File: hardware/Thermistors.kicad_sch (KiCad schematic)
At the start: 10 parts, among them J1 Conn_01x08

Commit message: updated sheets and 1st review changes
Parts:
- removed J1: Conn_01x08, symbol Connector_Generic:Conn_01x08
- removed R93, R94, R95, R96: 10k, symbol Device:R_Small
- added C1, C10, C11, C12, C2, C7, C8, C9: 1uF, symbol Device:C_Small
- added R33, R37, R38, R43, R44, R49, R50: 15k, symbol Device:R_Small
- added R34, R39, R40, R45, R46, R51, R52: 3.6k, symbol Device:R_Small
- added R35, R36, R41, R42, R47, R48: 1k, symbol Device:R_Small
- R29: value 10k -> 3.6k
- R30: value 10k -> 15k
- R31, R32: value 10k -> 1k
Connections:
- net NTC0: now also R48.1, R50.2, R52.1
- net NTC1: now also R47.1, R49.2, R51.1
- net NTC2: now also R42.1, R44.2, R46.1
- net NTC3: now also R41.1, R43.2, R45.1
- net NTC4: now also R36.1, R38.2, R40.1; no longer R32.1
- net NTC5: now also R35.1, R37.2, R39.1; no longer R31.1
- net NTC6: now also R32.1, R33.2, R34.1; no longer R30.1
- net NTC7: now also R30.2, R31.1
- net TSREF: now also R34.2, R39.2, R40.2, R45.2, R46.2, R51.2, R52.2; no longer R30.2, R31.2, R32.2
- net GNDA renamed AVSS
- net AVSS: now also R30.1, C1.2, C10.2, C11.2, C12.2, C2.2, C7.2, C8.2, C9.2, R33.1, R37.1, R38.1, R43.1, R44.1, R49.1, R50.1
- new net TEMP_0: C12.1, R48.2
- new net TEMP_1: C11.1, R47.2
- new net TEMP_2: C10.1, R42.2
- new net TEMP_3: C9.1, R41.2
- new net TEMP_4: C8.1, R36.2
- new net TEMP_5: C7.1, R35.2
- new net TEMP_6: C2.1, R32.2
- new net TEMP_7: C1.1, R31.2
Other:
- removed sheet 3V3_LDO
- removed sheet Temp Filters1
- moved on the sheet: C127

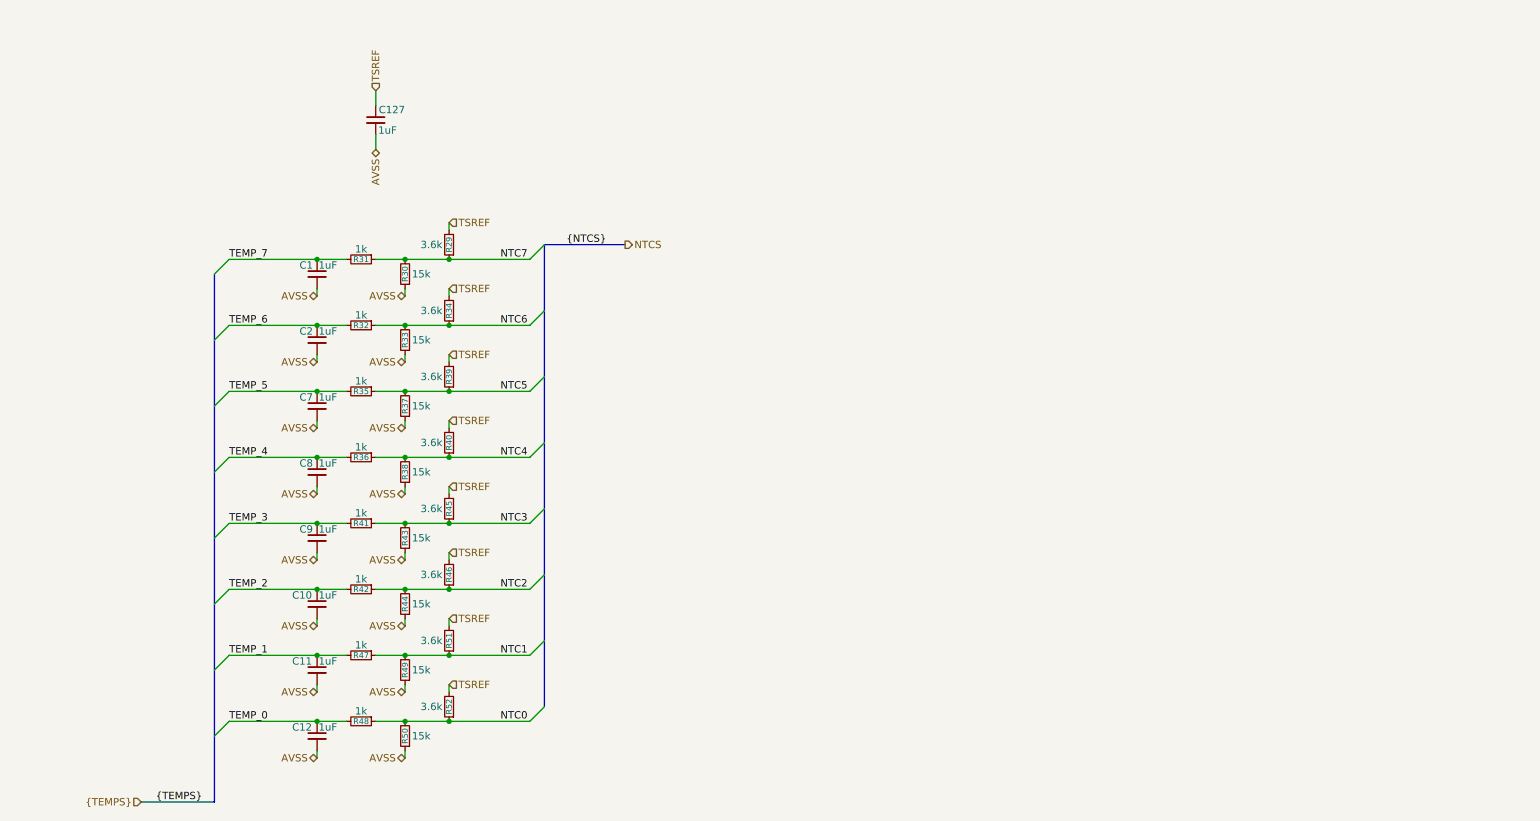
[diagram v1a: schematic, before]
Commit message: updated sheets, footprint, and calcs; 2nd review changes
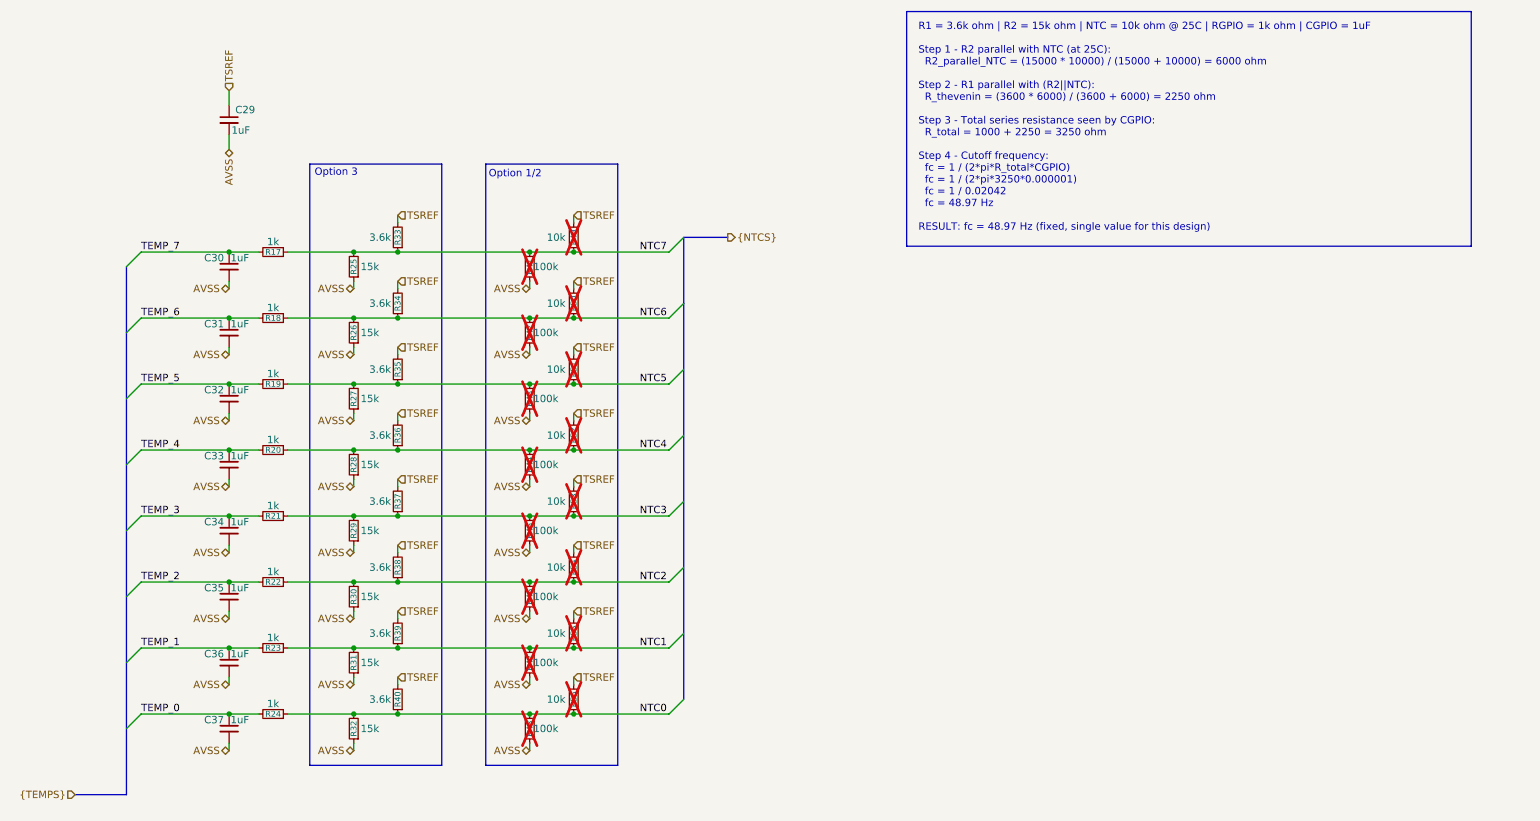
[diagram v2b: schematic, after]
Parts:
- added R41, R42, R43, R44, R45, R46, R47, R48: 100k, Resistor_SMD:R_0603_1608Metric_Pad0.98x0.95mm_HandSolder, symbol Device:R_Small
- added R49, R50, R51, R52, R53, R54, R55, R56: 10k, Resistor_SMD:R_0603_1608Metric_Pad0.98x0.95mm_HandSolder, symbol Device:R_Small
- C29: renamed from C127; footprint (none) -> Capacitor_SMD:C_0603_1608Metric_Pad1.08x0.95mm_HandSolder
- C30: renamed from C1; footprint (none) -> Capacitor_SMD:C_0603_1608Metric_Pad1.08x0.95mm_HandSolder
- C31: renamed from C2; footprint (none) -> Capacitor_SMD:C_0603_1608Metric_Pad1.08x0.95mm_HandSolder
- C32: renamed from C7; footprint (none) -> Capacitor_SMD:C_0603_1608Metric_Pad1.08x0.95mm_HandSolder
- C33: renamed from C8; footprint (none) -> Capacitor_SMD:C_0603_1608Metric_Pad1.08x0.95mm_HandSolder
- C34: renamed from C9; footprint (none) -> Capacitor_SMD:C_0603_1608Metric_Pad1.08x0.95mm_HandSolder
- C35: renamed from C10; footprint (none) -> Capacitor_SMD:C_0603_1608Metric_Pad1.08x0.95mm_HandSolder
- C36: renamed from C11; footprint (none) -> Capacitor_SMD:C_0603_1608Metric_Pad1.08x0.95mm_HandSolder
- C37: renamed from C12; footprint (none) -> Capacitor_SMD:C_0603_1608Metric_Pad1.08x0.95mm_HandSolder
- R17: renamed from R31; footprint (none) -> Resistor_SMD:R_0603_1608Metric_Pad0.98x0.95mm_HandSolder
- R18: renamed from R32; footprint (none) -> Resistor_SMD:R_0603_1608Metric_Pad0.98x0.95mm_HandSolder
- R19: renamed from R35; footprint (none) -> Resistor_SMD:R_0603_1608Metric_Pad0.98x0.95mm_HandSolder
- R20: renamed from R36; footprint (none) -> Resistor_SMD:R_0603_1608Metric_Pad0.98x0.95mm_HandSolder
- R21: renamed from R41; footprint (none) -> Resistor_SMD:R_0603_1608Metric_Pad0.98x0.95mm_HandSolder
- R22: renamed from R42; footprint (none) -> Resistor_SMD:R_0603_1608Metric_Pad0.98x0.95mm_HandSolder
- R23: renamed from R47; footprint (none) -> Resistor_SMD:R_0603_1608Metric_Pad0.98x0.95mm_HandSolder
- R24: renamed from R48; footprint (none) -> Resistor_SMD:R_0603_1608Metric_Pad0.98x0.95mm_HandSolder
- R25: renamed from R30; footprint (none) -> Resistor_SMD:R_0603_1608Metric_Pad0.98x0.95mm_HandSolder
- R26: renamed from R33; footprint (none) -> Resistor_SMD:R_0603_1608Metric_Pad0.98x0.95mm_HandSolder
- R27: renamed from R37; footprint (none) -> Resistor_SMD:R_0603_1608Metric_Pad0.98x0.95mm_HandSolder
- R28: renamed from R38; footprint (none) -> Resistor_SMD:R_0603_1608Metric_Pad0.98x0.95mm_HandSolder
- R29: renamed from R43; footprint (none) -> Resistor_SMD:R_0603_1608Metric_Pad0.98x0.95mm_HandSolder
- R30: renamed from R44; footprint (none) -> Resistor_SMD:R_0603_1608Metric_Pad0.98x0.95mm_HandSolder
- R31: renamed from R49; footprint (none) -> Resistor_SMD:R_0603_1608Metric_Pad0.98x0.95mm_HandSolder
- R32: renamed from R50; footprint (none) -> Resistor_SMD:R_0603_1608Metric_Pad0.98x0.95mm_HandSolder
- R33: renamed from R29; footprint (none) -> Resistor_SMD:R_0603_1608Metric_Pad0.98x0.95mm_HandSolder
- R34: footprint (none) -> Resistor_SMD:R_0603_1608Metric_Pad0.98x0.95mm_HandSolder
- R35: renamed from R39; footprint (none) -> Resistor_SMD:R_0603_1608Metric_Pad0.98x0.95mm_HandSolder
- R36: renamed from R40; footprint (none) -> Resistor_SMD:R_0603_1608Metric_Pad0.98x0.95mm_HandSolder
- R37: renamed from R45; footprint (none) -> Resistor_SMD:R_0603_1608Metric_Pad0.98x0.95mm_HandSolder
- R38: renamed from R46; footprint (none) -> Resistor_SMD:R_0603_1608Metric_Pad0.98x0.95mm_HandSolder
- R39: renamed from R51; footprint (none) -> Resistor_SMD:R_0603_1608Metric_Pad0.98x0.95mm_HandSolder
- R40: renamed from R52; footprint (none) -> Resistor_SMD:R_0603_1608Metric_Pad0.98x0.95mm_HandSolder
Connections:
- net AVSS: now also R41.1, R42.1, R43.1, R44.1, R45.1, R46.1, R47.1, R48.1
- net NTC0: now also R48.2, R56.1
- net NTC1: now also R47.2, R55.1
- net NTC2: now also R46.2, R54.1
- net NTC3: now also R45.2, R53.1
- net NTC4: now also R44.2, R52.1
- net NTC5: now also R43.2, R51.1
- net NTC6: now also R42.2, R50.1
- net NTC7: now also R41.2, R49.1
- net TSREF: now also R49.2, R50.2, R51.2, R52.2, R53.2, R54.2, R55.2, R56.2
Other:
- note added: "Option 1/2"
- note added: "Option 3"
- note added: "R1 = 3.6k ohm | R2 = 15k ohm | NTC = 10k ohm @ 25C | RGPIO = 1k ohm | CGPIO = 1uF Step 1 - R2 parallel with NTC (at 25C): R2_parallel_NTC = (15000 * 10000) / (15000 + 10000) = 6000 ohm Step 2 - R1 parallel with (R2||NTC): R_thevenin = (3600 * 6000) / (3600 + 6000) = 2250 ohm Step 3 - Total series resistance seen by CGPIO: R_total = 1000 + 2250 = 3250 ohm Step 4 - Cutoff frequency: fc = 1 / (2*pi*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"
- moved on the sheet: C29, C30, C31, C32, C33, C34, C35, C36, C37, R17, R18, R19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
